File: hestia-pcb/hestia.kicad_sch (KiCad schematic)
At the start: 76 parts, among them J1 Serial Connector, J2 i2c connector, J5 VREF+, J6 Conn_02x07_Odd_Even, SW1 SW_Push, U2 MSP430F2618TPN_Simplifed, U3 ADS7828, U8 TXB0104PW, U9 LTC4313-1, Y1 32.768kHz 12.5pf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

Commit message: added new themal switch footprint to hestia lib. Added 3 wire restraint hole footprints -> 1.2mm, 1.8mm and 1.9mm. Change adc wire restraint holes (H9 to H13) to 1.8mm. Change uC wire restraint holes(H14 & H15) to 1.8mm & moved H14 & H15 designators. Change thermal switch wire restraint holes (H16 & H17) to 1.9mm & also shifted hole coords left 0.2mm & moved H16 & H17 designators. Change thermal switch footprint to new footprint with thruhole pads to 1.2mm dia hole as well as with increased pad distance. Thicken VCC traces to thermal switch - have to revisit to satisfy DRC - probably change multiple traces to signal polygon. Added two GND vias for extra GND stitching off J2. ToDo -Resolve DRC issues. Some padd may need extra signal spurs to pads - just manually adding a trace to the pads may satisfy the DRC requirement
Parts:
- H10, H11, H12, H13, H14, H15, H9: footprint Hestia:Wire_Restraint_Hole -> Hestia:Wire_Restraint_Hole_1.8mm
- H16, H17: footprint Hestia:Wire_Restraint_Hole -> Hestia:Wire_Restraint_Hole_1.9mm
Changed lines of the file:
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@@
       (effects (font (size 1.27 1.27)) (justify left) hide)
     )
-    (property "Footprint" "Hestia:Wire_Restraint_Hole" (at 153.035 172.72 0)
+    (property "Footprint" "Hestia:Wire_Restraint_Hole_1.8mm" (at 153.035 172.72 0)
       (effects (font (size 1.27 1.27)) hide)
     )
@@
       (effects (font (size 1.27 1.27)) (justify left))
     )
-    (property "Footprint" "Hestia:Wire_Restraint_Hole" (at 153.035 165.735 0)
+    (property "Footprint" "Hestia:Wire_Restraint_Hole_1.8mm" (at 153.035 165.735 0)
       (effects (font (size 1.27 1.27)) hide)
     )
@@
       (effects (font (size 1.27 1.27)) (justify left) hide)
     )
-    (property "Footprint" "Hestia:Wire_Restraint_Hole" (at 167.005 172.72 0)
+    (property "Footprint" "Hestia:Wire_Restraint_Hole_1.8mm" (at 167.005 172.72 0)
       (effects (font (size 1.27 1.27)) hide)
     )
@@
       (effects (font (size 1.27 1.27)) (justify left) hide)
     )
-    (property "Footprint" "Hestia:Wire_Restraint_Hole" (at 162.56 172.72 0)
+    (property "Footprint" "Hestia:Wire_Restraint_Hole_1.8mm" (at 162.56 172.72 0)
       (effects (font (size 1.27 1.27)) hide)
     )
@@
       (effects (font (size 1.27 1.27)) (justify left) hide)
     )
-    (property "Footprint" "Hestia:Wire_Restraint_Hole" (at 162.56 165.735 0)
+    (property "Footprint" "Hestia:Wire_Restraint_Hole_1.8mm" (at 162.56 165.735 0)
       (effects (font (size 1.27 1.27)) hide)
     )
@@
       (effects (font (size 1.27 1.27)) (justify left) hide)
     )
-    (property "Footprint" "Hestia:Wire_Restraint_Hole" (at 171.45 165.735 0)
+    (property "Footprint" "Hestia:Wire_Restraint_Hole_1.9mm" (at 171.45 165.735 0)
       (effects (font (size 1.27 1.27)) hide)
     )
@@
       (effects (font (size 1.27 1.27)) (justify left) hide)
     )
-    (property "Footprint" "Hestia:Wire_Restraint_Hole" (at 157.48 172.72 0)
+    (property "Footprint" "Hestia:Wire_Restraint_Hole_1.8mm" (at 157.48 172.72 0)
       (effects (font (size 1.27 1.27)) hide)
     )
@@
       (effects (font (size 1.27 1.27)) (justify left) hide)
     )
-    (property "Footprint" "Hestia:Wire_Restraint_Hole" (at 157.48 165.735 0)
+    (property "Footprint" "Hestia:Wire_Restraint_Hole_1.8mm" (at 157.48 165.735 0)
       (effects (font (size 1.27 1.27)) hide)
     )
@@
       (effects (font (size 1.27 1.27)) (justify left) hide)
     )
-    (property "Footprint" "Hestia:Wire_Restraint_Hole" (at 167.005 165.735 0)
-      (effects (font (size 1.27 1.27)) hide)
-    )
+    (property "Footprint" "Hestia:Wire_Restraint_Hole_1.9mm" (at 167.005 165.735 0)
+      (effects (font (size 1.27 1.27)) hide)
+    )

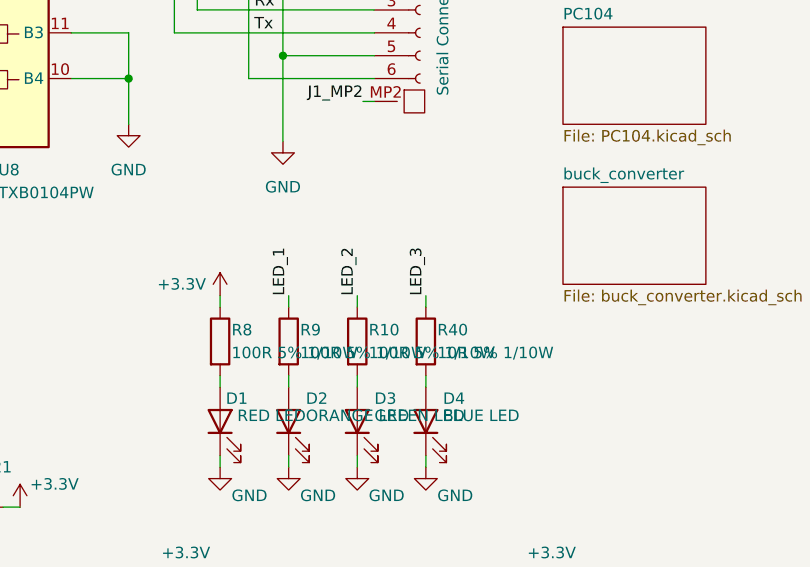
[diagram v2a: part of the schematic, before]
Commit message: change R40 (blue LED current limiting resistor) schematic value to 100R as was specified for it's digikey resistor part number. It had been agreed that the blue LED intensity at 100R was acceptable
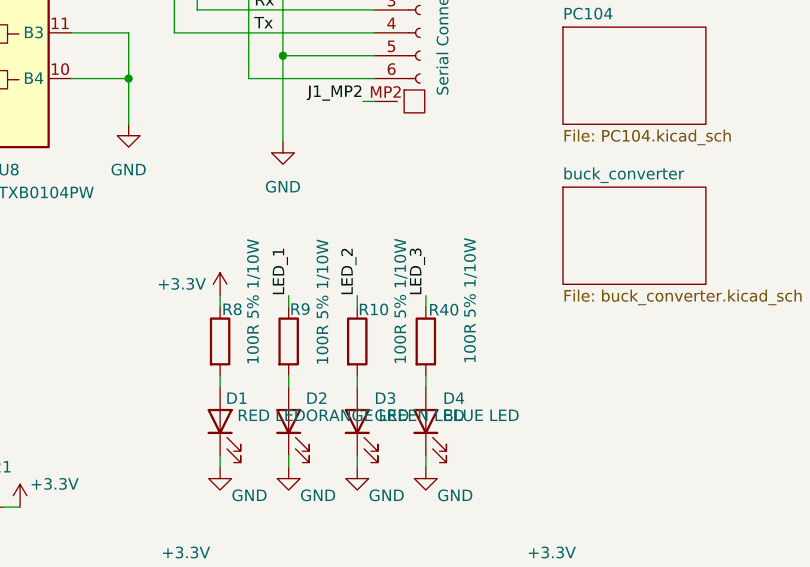
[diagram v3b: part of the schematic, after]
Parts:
- R40: value 10R 5% 1/10W -> 100R 5% 1/10W
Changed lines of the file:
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@@
   (symbol (lib_id "Device:R") (at 227.33 92.075 0) (unit 1)
     (in_bom yes) (on_board yes) (dnp no)
-    (property "Reference" "R9" (at 228.6 90.805 0)
-      (effects (font (size 1.27 1.27)) (justify left))
-    )
-    (property "Value" "100R 5% 1/10W" (at 228.6 93.345 0)
+    (property "Reference" "R9" (at 227.4522 88.5223 0)
+      (effects (font (size 1.27 1.27)) (justify left))
+    )
+    (property "Value" "100R 5% 1/10W" (at 231.128 94.7362 90)
       (effects (font (size 1.27 1.27)) (justify left))
     )
@@
   (symbol (lib_id "Device:R") (at 242.57 92.075 0) (unit 1)
     (in_bom yes) (on_board yes) (dnp no)
-    (property "Reference" "R40" (at 243.84 90.805 0)
-      (effects (font (size 1.27 1.27)) (justify left))
-    )
-    (property "Value" "10R 5% 1/10W" (at 243.84 93.345 0)
+    (property "Reference" "R40" (at 242.864 88.5955 0)
+      (effects (font (size 1.27 1.27)) (justify left))
+    )
+    (property "Value" "100R 5% 1/10W" (at 247.5142 94.5694 90)
       (effects (font (size 1.27 1.27)) (justify left))
     )
@@
   (symbol (lib_id "Device:R") (at 234.95 92.075 0) (unit 1)
     (in_bom yes) (on_board yes) (dnp no)
-    (property "Reference" "R10" (at 236.22 90.805 0)
-      (effects (font (size 1.27 1.27)) (justify left))
-    )
-    (property "Value" "100R 5% 1/10W" (at 236.22 93.345 0)
+    (property "Reference" "R10" (at 235.0664 88.566 0)
+      (effects (font (size 1.27 1.27)) (justify left))
+    )
+    (property "Value" "100R 5% 1/10W" (at 239.7706 94.6487 90)
       (effects (font (size 1.27 1.27)) (justify left))
     )
@@
   (symbol (lib_id "Device:R") (at 219.71 92.075 0) (unit 1)
     (in_bom yes) (on_board yes) (dnp no)
-    (property "Reference" "R8" (at 220.98 90.805 0)
-      (effects (font (size 1.27 1.27)) (justify left))
-    )
-    (property "Value" "100R 5% 1/10W" (at 220.98 93.345 0)
-      (effects (font (size 1.27 1.27)) (justify left))
-    )
+    (property "Reference" "R8" (at 219.9036 88.5442 0)
+      (effects (font (size 1.27 1.27)) (justify left))
+    )
+    (property "Value" "100R 5% 1/10W" (at 223.4044 94.6924 90)
+      (effects (font (size 1.27 1.27)) (justify left))
+    )

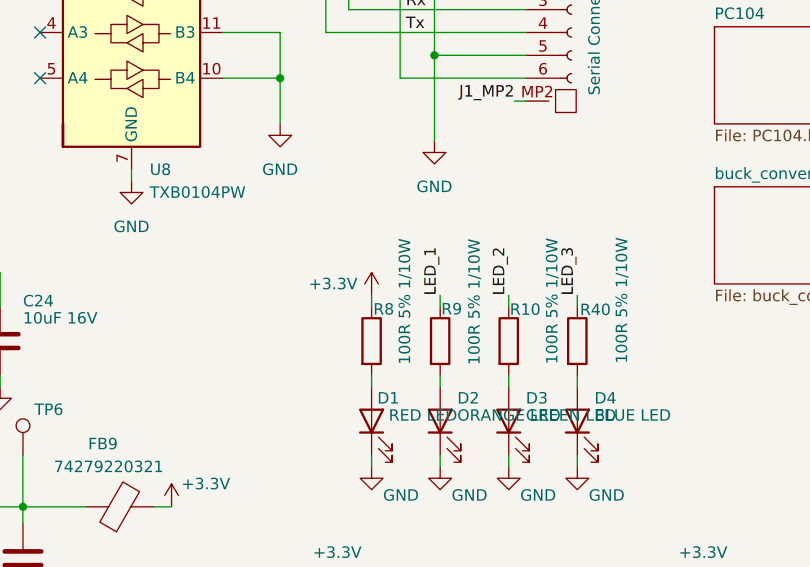
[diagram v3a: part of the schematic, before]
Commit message: change R8 (red led current limiting resistor) value from 100R to 180R to reduce intensity. Digikey part number for R8 changed for a 180R resistor
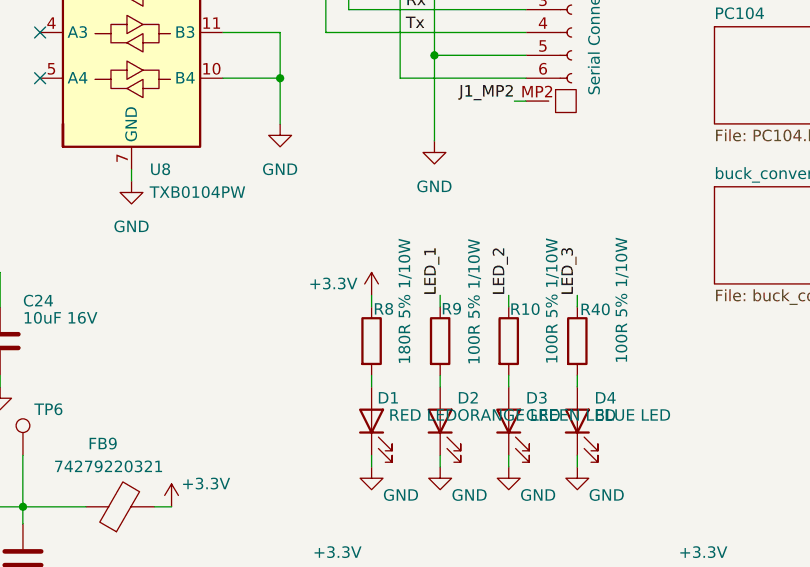
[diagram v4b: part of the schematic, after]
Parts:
- R8: value 100R 5% 1/10W -> 180R 5% 1/10W; Digikey Part 13-RC0603JR-13100RLCT-ND -> 311-180GRCT-ND
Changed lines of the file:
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@@
       (effects (font (size 1.27 1.27)) (justify left))
     )
-    (property "Value" "100R 5% 1/10W" (at 223.4044 94.6924 90)
+    (property "Value" "180R 5% 1/10W" (at 223.4044 94.6924 90)
       (effects (font (size 1.27 1.27)) (justify left))
     )
@@
       (effects (font (size 1.27 1.27)) hide)
     )
-    (property "Digikey Part" "13-RC0603JR-13100RLCT-ND" (at 219.71 92.075 0)
+    (property "Digikey Part" "311-180GRCT-ND" (at 219.71 92.075 0)
       (effects (font (size 1.27 1.27)) hide)
     )

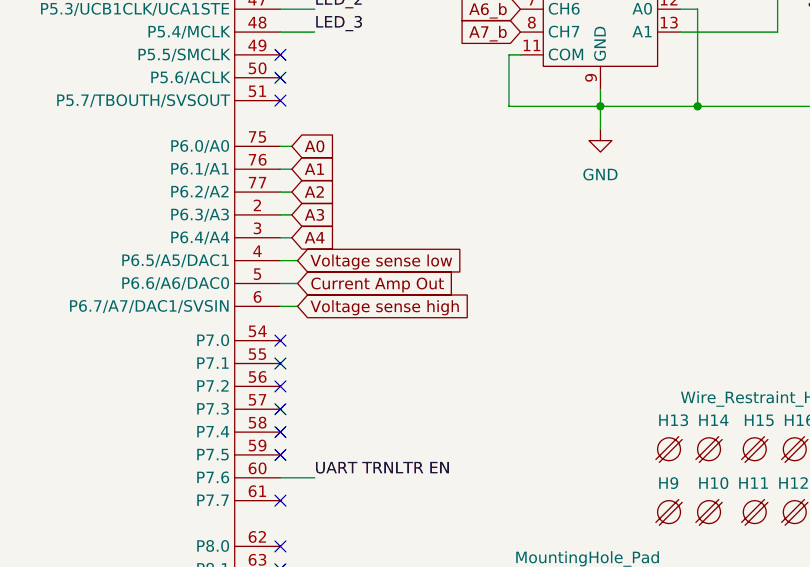
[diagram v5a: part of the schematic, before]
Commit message: reroute current amp out with option resistor to current amp in to directly measure voltage on that side of the current sense resistor. Via added to assist that signal route. add series resistor to current sense line towards uC for current limiting in the case that the low side of the current limiting resistor is experiencing 5V.
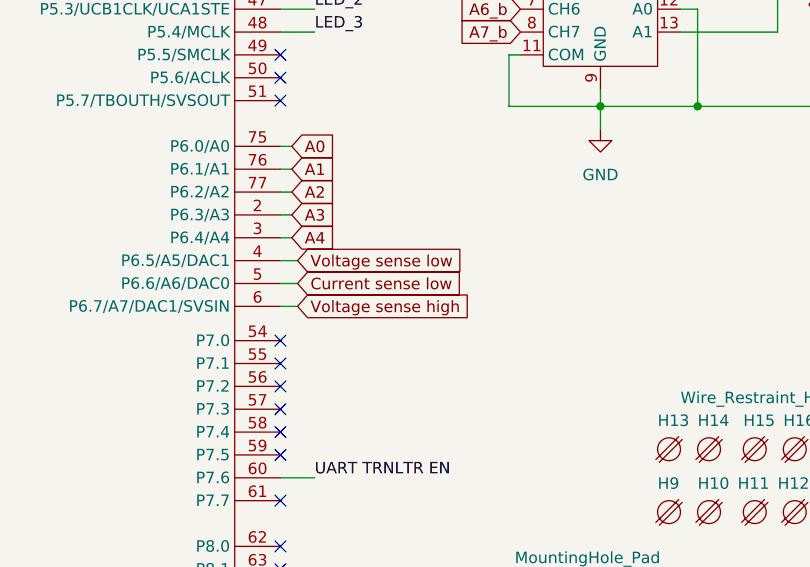
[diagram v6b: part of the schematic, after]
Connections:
- net Current Amp Out renamed Current sense low
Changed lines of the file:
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@@
     )
   )
-  (global_label "Current Amp Out" (shape input) (at 111.76 147.32 0) (fields_autoplaced)
+  (global_label "Current sense low" (shape input) (at 111.76 147.32 0) (fields_autoplaced)
     (effects (font (size 1.27 1.27)) (justify left))
-    (property "Intersheetrefs" "${INTERSHEET_REFS}" (at 130.1993 147.2406 0)
+    (property "Intersheetrefs" "${INTERSHEET_REFS}" (at 132.0828 147.32 0)
       (effects (font (size 1.27 1.27)) (justify left) hide)
     )
